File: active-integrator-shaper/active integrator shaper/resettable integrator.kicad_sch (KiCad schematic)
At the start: 0 parts

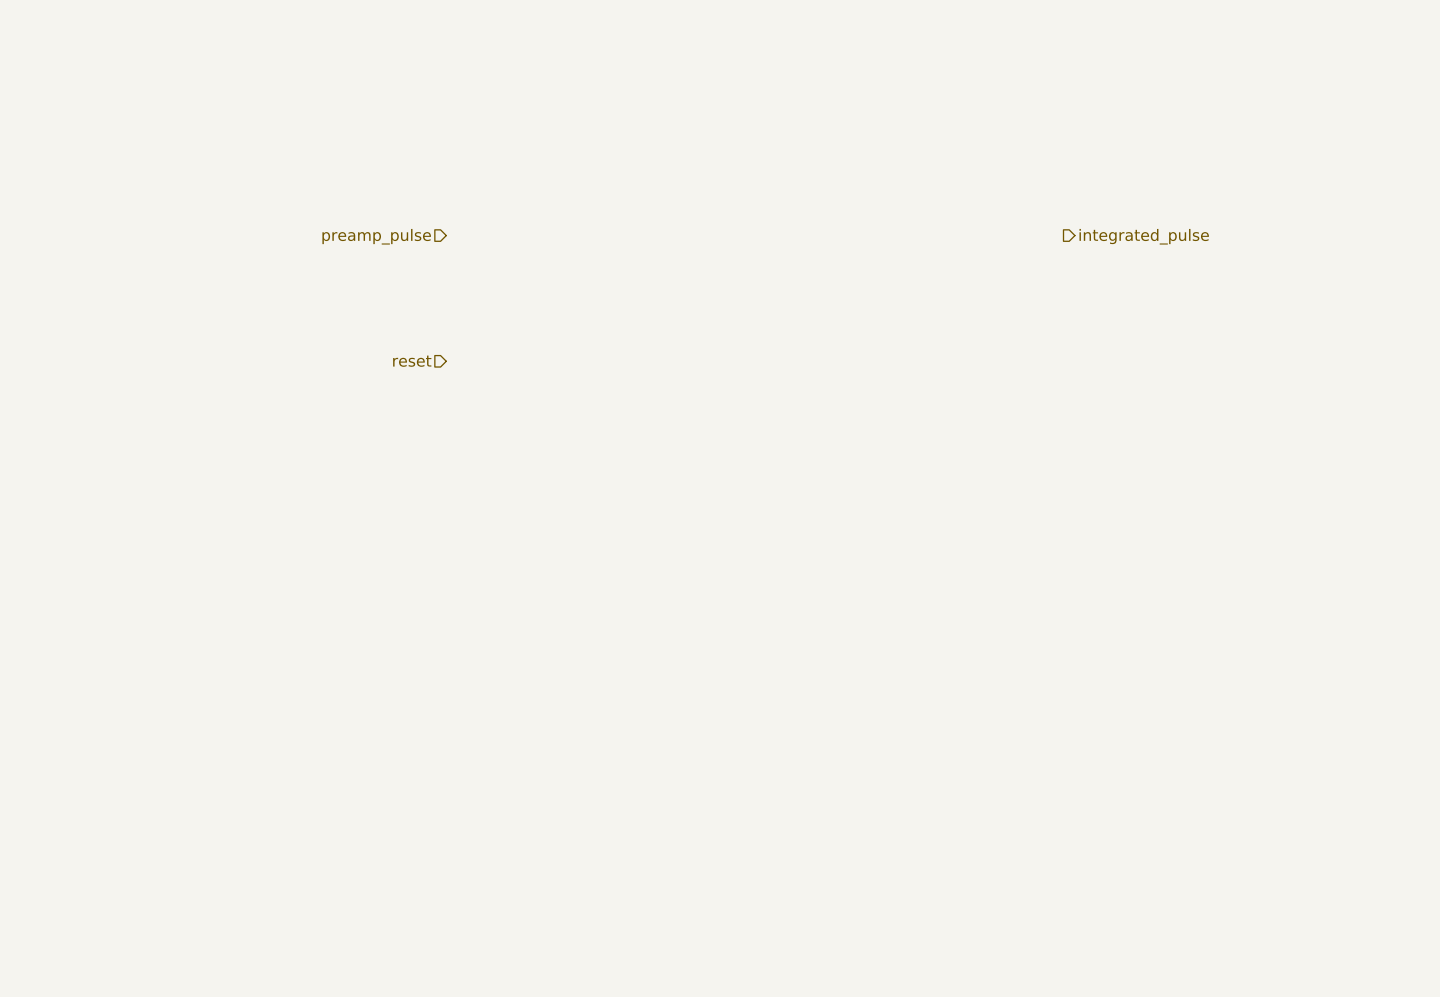
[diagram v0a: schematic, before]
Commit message: add integration portion
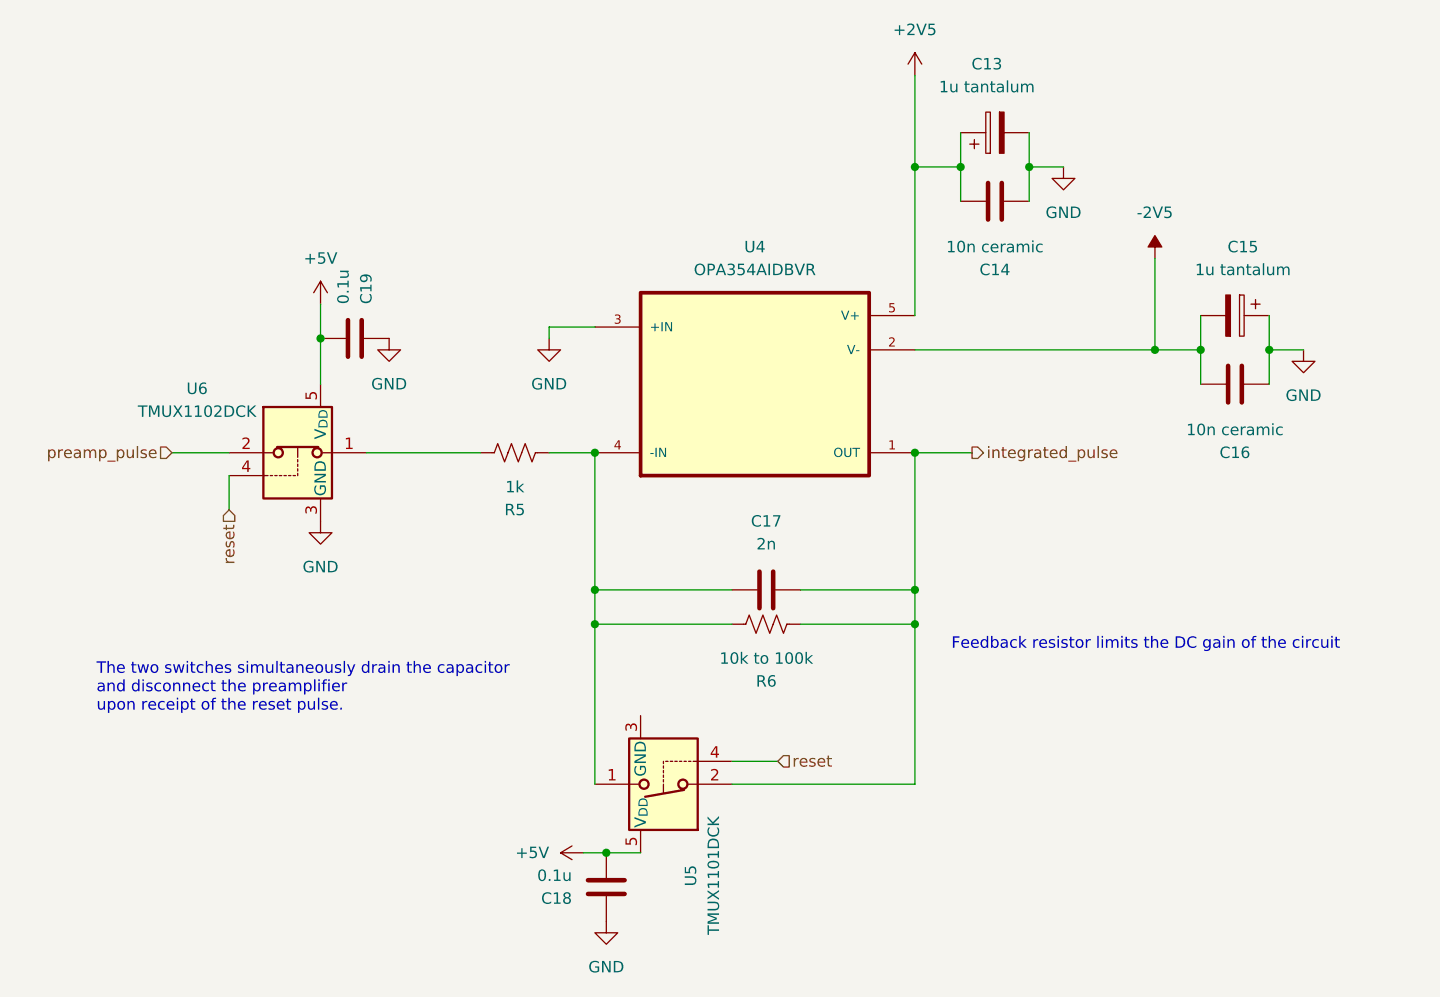
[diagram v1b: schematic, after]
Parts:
- added C13, C15: 1u tantalum, Capacitor_SMD:C_1206_3216Metric_Pad1.33x1.80mm_HandSolder, symbol Device:C_Polarized
- added C14, C16: 10n ceramic, Capacitor_SMD:C_1206_3216Metric_Pad1.33x1.80mm_HandSolder, symbol Device:C
- added C17: 2n, Capacitor_SMD:C_0805_2012Metric_Pad1.18x1.45mm_HandSolder, symbol Device:C
- added C18, C19: 0.1u, symbol Device:C
- added R5: 1k, Resistor_SMD:R_0805_2012Metric_Pad1.20x1.40mm_HandSolder, symbol Device:R_US
- added R6: 10k to 100k, Resistor_SMD:R_0805_2012Metric_Pad1.20x1.40mm_HandSolder, symbol Device:R_US
- added U4: OPA354AIDBVR, Package_TO_SOT_SMD:SOT-23-5, symbol Library:OPA354AIDBVR
- added U5: TMUX1101DCK, Package_TO_SOT_SMD:SOT-23-5, symbol Analog_Switch:TMUX1101DCK
- added U6: TMUX1102DCK, Package_TO_SOT_SMD:SOT-23-5, symbol Analog_Switch:TMUX1102DCK
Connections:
- net integrated_pulse: now also C17.2, R6.1, U4.1 (OUT), U5.2
- net preamp_pulse: now also U6.2
- net reset: now also U5.4, U6.4
- new net: C17.1, R5.1, R6.2, U4.4 (-IN), U5.1
- new net: R5.2, U6.1
- new net +2V5: C13.1, C14.1, U4.5 (V+)
- new net +5V: C18.1, C19.1, U5.5 (V_{DD}), U6.5 (V_{DD})
- new net -2V5: C15.2, C16.1, U4.2 (V-)
- new net GND: C13.2, C14.2, C15.1, C16.2, C18.2, C19.2, U4.3 (+IN), U6.3 (GND)
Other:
- note added: "Feedback resistor limits the DC gain of the circuit"
- note added: "The two switches simultaneously drain the capacitor and disconnect the preamplifier upon receipt of the reset pulse."
